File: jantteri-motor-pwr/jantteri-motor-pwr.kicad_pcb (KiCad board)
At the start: 2 copper layers, 40 x 80.6 mm, 56 parts, among them J1 Conn_01x06_Male, J2 SWD, J3 DBG, J4 POT, J5 12V, J6 PWR-SW, J7 M, Q1 PDN3909S, Q2 IRLML6402TRPBF, Q3 IRLML6402TRPBF, U1 lora-mod, U2 STM32G030C8T6, U3 AP2301, U4 AMS1117-3.3, U5 AP2301, U6 LM2596S-5, U7 DRV8848, Y1 16MHz

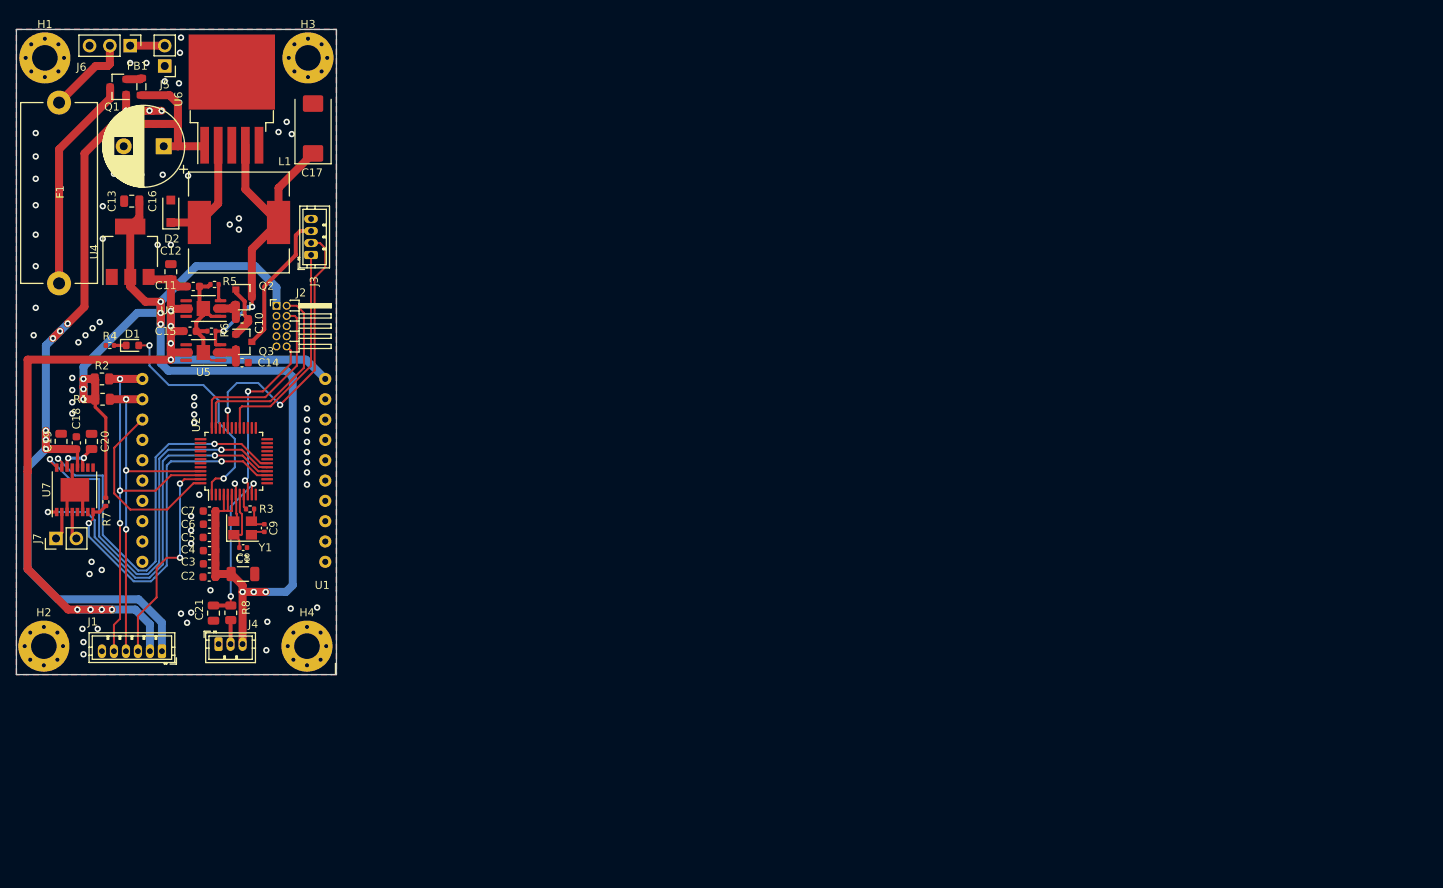
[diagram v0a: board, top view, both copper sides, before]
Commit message: motor-pwrv2
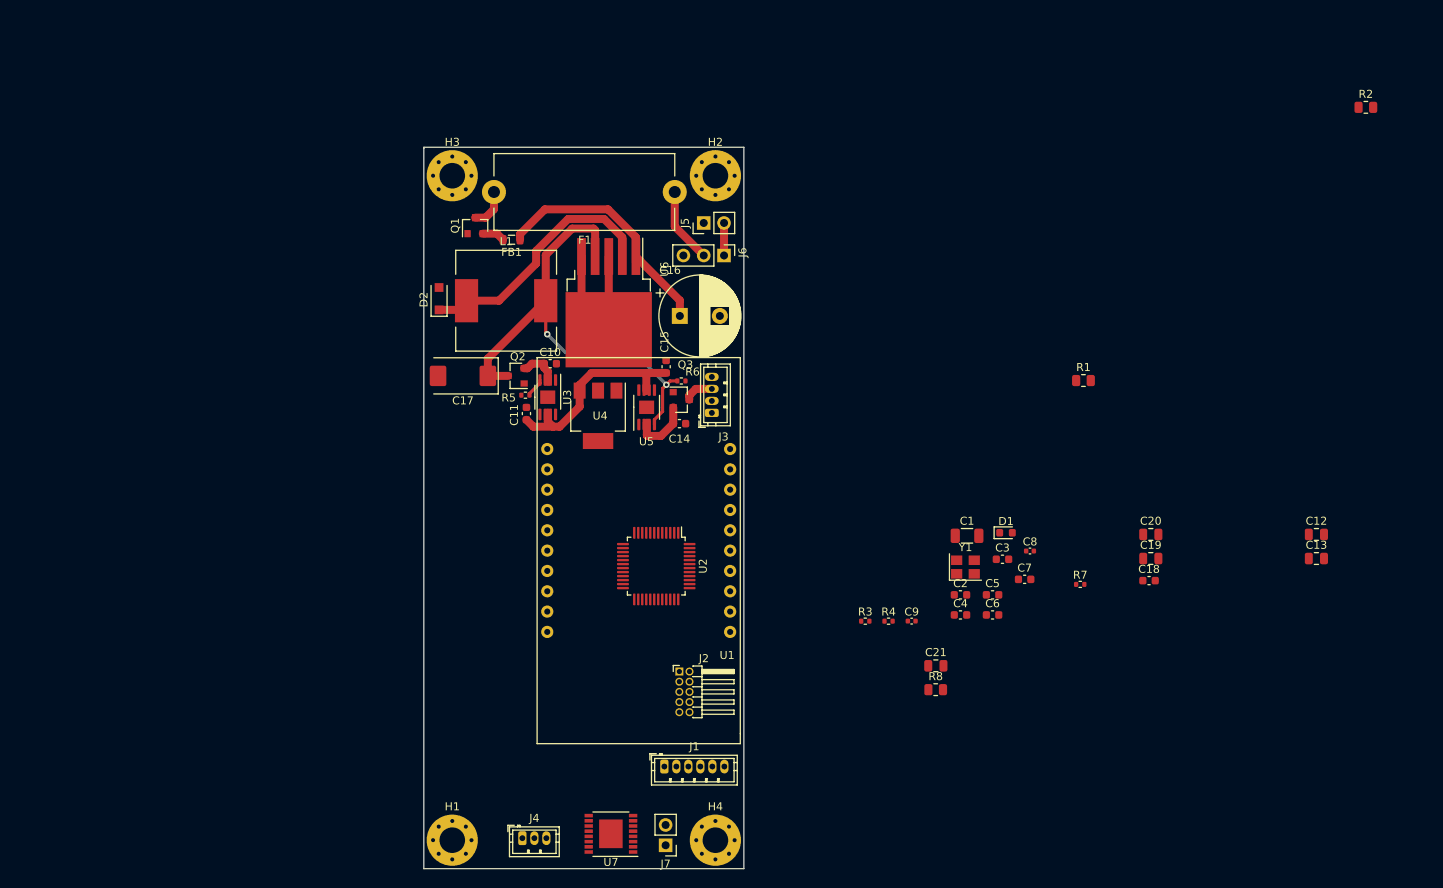
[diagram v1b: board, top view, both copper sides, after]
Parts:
- moved R2 161.6 mm to (194.1, 57.7)
- moved C13 154.7 mm to (187.9, 114.1), turned to 0 degrees
- moved C12 146.9 mm to (187.9, 111.1), turned to 0 degrees
- moved C19 137.0 mm to (167.2, 114.1), turned to 0 degrees
- moved C18 135.2 mm to (167.0, 116.9), turned to 0 degrees
- moved C20 132.9 mm to (167.2, 111.1), turned to 0 degrees
- moved R1 122.6 mm to (158.8, 91.9)
- moved R7 122.2 mm to (158.4, 117.4), turned to 0 degrees
- moved D1 111.7 mm to (149.1, 110.9)
- moved H1 110.3 mm to (79.9, 149.4)
- moved R4 103.3 mm to (134.4, 122.0)
- moved H2 102.5 mm to (112.8, 66.3)
- moved C7 102.3 mm to (151.4, 116.7), turned to 0 degrees
- moved C3 99.1 mm to (148.7, 114.2), turned to 0 degrees
- moved C6 98.5 mm to (147.4, 121.2), turned to 0 degrees
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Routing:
- net +3V3: track 164.0 -> 0.00 mm, vias 9 -> 0
- net +5V: track 119.1 -> 26.6 mm, vias 8 -> 0
- net +12V: track 116.5 -> 30.8 mm, vias 6 -> 0
- net MOTOR_A: track 53.7 -> 0.00 mm, vias 2 -> 0
- net MOTOR_B: track 52.8 -> 0.00 mm, vias 2 -> 0
- net SDA: track 49.4 -> 0.00 mm, vias 3 -> 0
- net DRV_SLEEP: track 47.8 -> 0.00 mm, vias 2 -> 0
- net SCL: track 44.9 -> 0.00 mm, vias 3 -> 0
- net DRV_FAULT: track 44.0 -> 0.00 mm, vias 2 -> 0
- net /jst-dbg/DBG_RX: track 36.6 -> 0.00 mm, vias 2 -> 0
- net Net-(D1-Pad2): track 28.7 -> 0.00 mm, vias 2 -> 0
- net /jst-dbg/DBG_TX: track 27.4 -> 0.00 mm
- net HIT_INT: track 26.9 -> 0.00 mm, vias 2 -> 0
- net /10pinARM/SWDIO: track 25.3 -> 0.00 mm
- net GND: track 43.8 -> 19.7 mm, vias 72 -> 0
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- removed copper zone on B.Cu, net GND
- removed copper zone on F.Cu, net GND
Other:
- board size 40 x 80.6 mm -> 40 x 90.2 mm

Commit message: revised motor-pwr
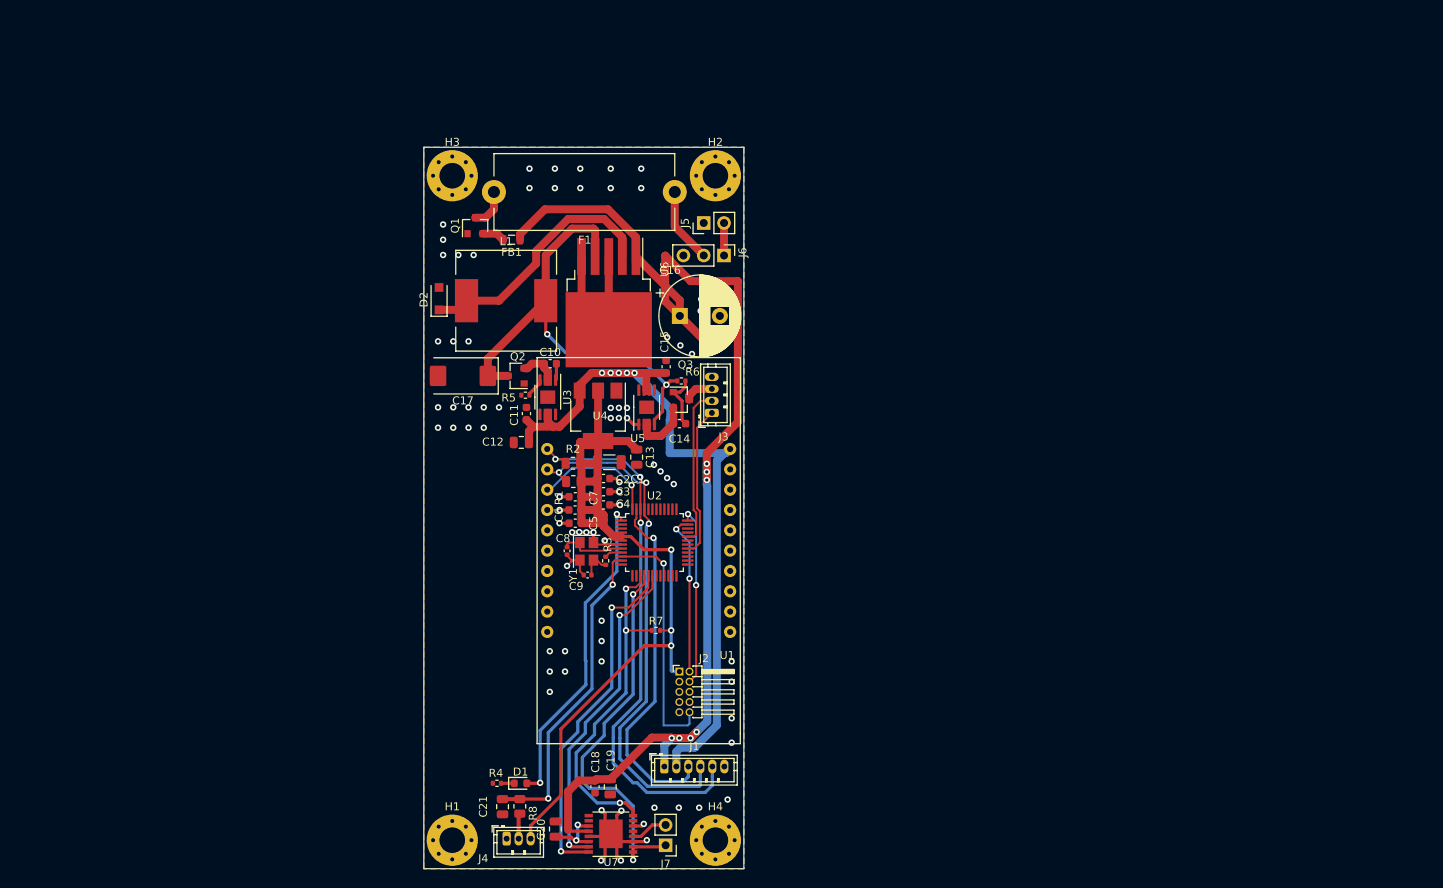
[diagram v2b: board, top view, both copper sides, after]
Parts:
- moved R2 108.6 mm to (95.0, 102.2), turned to 180 degrees
- moved C12 100.0 mm to (88.5, 99.6), turned to 180 degrees
- moved C13 85.9 mm to (102.9, 101.5), turned to 270 degrees
- moved C20 83.0 mm to (92.8, 148.0), turned to 270 degrees
- moved C18 73.9 mm to (97.7, 142.7), turned to 270 degrees
- moved C19 73.3 mm to (99.6, 142.7), turned to 270 degrees
- moved D1 68.3 mm to (88.4, 142.2)
- moved R1 65.0 mm to (95.0, 104.5), turned to 180 degrees
- moved C8 57.9 mm to (94.2, 113.2), turned to 270 degrees
- moved C7 57.1 mm to (95.3, 106.4), turned to 180 degrees
- moved C21 57.0 mm to (86.2, 145.2), turned to 270 degrees
- moved R8 54.0 mm to (88.3, 145.1), turned to 270 degrees
- moved C6 53.8 mm to (95.2, 108.1), turned to 180 degrees
- moved R7 53.3 mm to (105.3, 123.1)
- moved R4 53.0 mm to (85.5, 142.2)
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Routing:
- net +12V: track 30.8 -> 156.2 mm, vias 0 -> 7
- net +3V3: track 0.00 -> 109.7 mm, vias 0 -> 3
- net +5V: track 26.6 -> 96.2 mm, vias 0 -> 5
- net SDA: track 0.00 -> 68.5 mm, vias 0 -> 3
- net SCL: track 0.00 -> 65.8 mm, vias 0 -> 3
- net GND: track 19.7 -> 69.9 mm, vias 0 -> 72
- net DRV_SLEEP: track 0.00 -> 44.7 mm, vias 0 -> 2
- net HIT_INT: track 0.00 -> 44.3 mm, vias 0 -> 1
- net MOTOR_A: track 0.00 -> 43.7 mm, vias 0 -> 2
- net DRV_FAULT: track 0.00 -> 42.2 mm, vias 0 -> 3
- net MOTOR_B: track 0.00 -> 41.0 mm, vias 0 -> 2
- net Net-(D1-Pad2): track 0.00 -> 40.3 mm, vias 0 -> 2
- net POT: track 0.00 -> 39.8 mm, vias 0 -> 2
- net /10pinARM/NRST: track 0.00 -> 30.7 mm, vias 0 -> 1
- net /10pinARM/SWCLK: track 0.00 -> 22.5 mm, vias 0 -> 2
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- added copper zone on B.Cu, net GND
- added copper zone on F.Cu, net GND

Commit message: random changes
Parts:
- removed F1: C58066, Fuse:Fuseholder_Cylinder-5x20mm_Stelvio-Kontek_PTF78_Horizontal_Open
- moved D2 26.5 mm to (98.5, 64.5), turned to 0 degrees
- moved C17 24.5 mm to (88.7, 68.0)
- moved Q1 24.0 mm to (105.8, 65.9), turned to 270 degrees
- moved C12 18.4 mm to (103.1, 88.3), turned to 270 degrees
- moved FB1 17.6 mm to (102.9, 66.0), turned to 90 degrees
- moved C11 9.32 mm to (96.2, 89.9), turned to 180 degrees
- moved U3 9.06 mm to (97.9, 87.2), turned to 0 degrees
- moved U6 5.91 mm to (99.5, 76.3)
- moved Q2 4.90 mm to (90.3, 87.1)
- moved R5 4.89 mm to (92.0, 89.9)
- moved L1 4.45 mm to (86.6, 77.5)
- moved C10 2.62 mm to (93.0, 87.3), turned to 270 degrees
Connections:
- J6 pad 2: Net-(F1-Pad1) -> PWR+
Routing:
- net +12V: track 156.2 -> 112.4 mm
- net Net-(F1-Pad1): track 9.44 -> 0.00 mm
- net PWR+: track 4.94 -> 12.2 mm
- net +5V: track 96.2 -> 92.1 mm
- net Net-(D2-Pad1): track 31.9 -> 30.2 mm
- net /power_protect/EN: track 2.44 -> 3.87 mm
- net GND: track 69.9 -> 68.6 mm, vias 72 -> 93
- net Net-(FB1-Pad2): track 2.86 -> 1.97 mm
- net (no net): vias 5 -> 0
